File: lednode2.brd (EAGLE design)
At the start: 99.8 x 49.8 mm, 47 parts, among them Q1 AO3402, Q2 AO3402, Q3 AO3402, Q4 AO3402, Q5 AO3402, Q6 AO3402

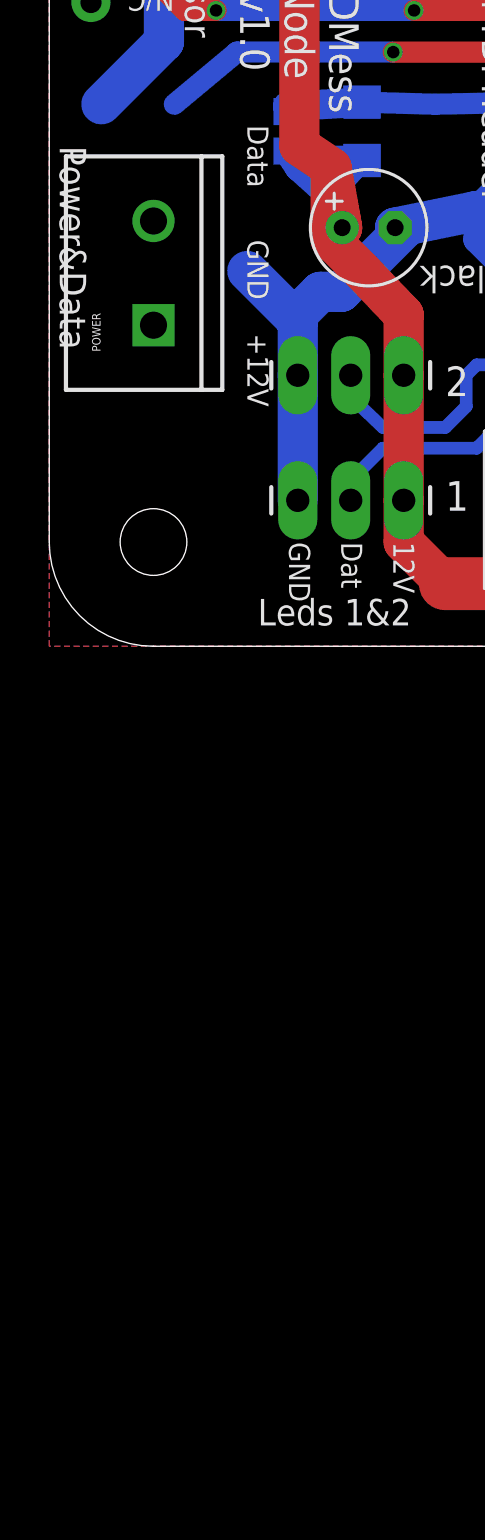
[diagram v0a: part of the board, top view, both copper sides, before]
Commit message: Working on new node version.
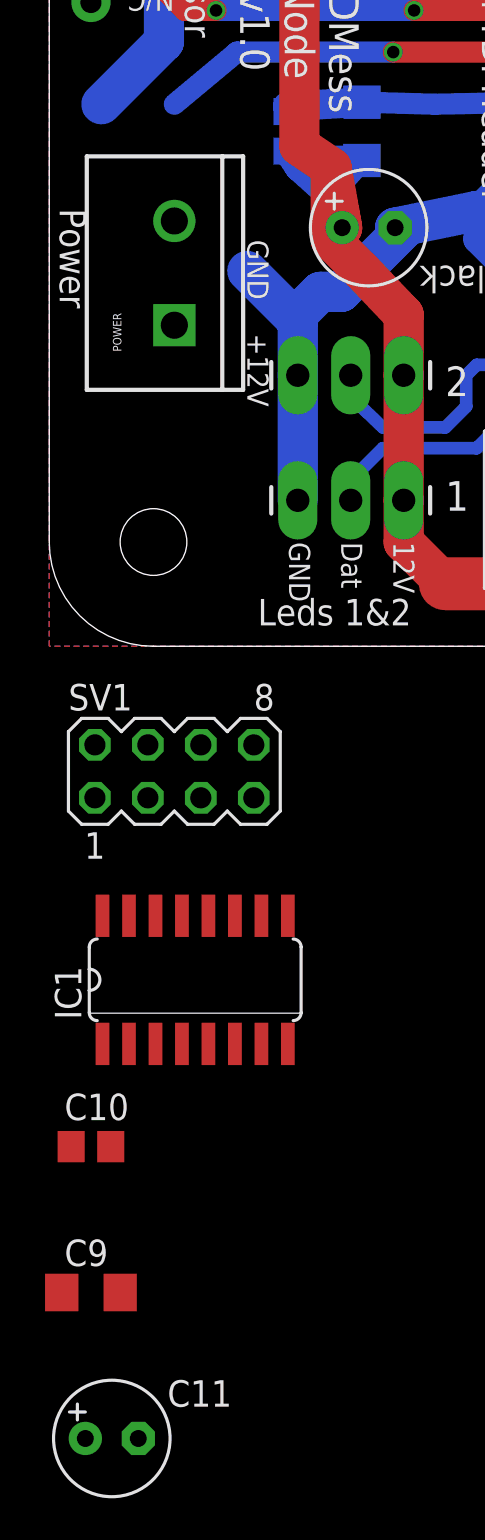
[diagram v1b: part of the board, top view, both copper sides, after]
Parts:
- added C10: 100 nF, rcl:C0805
- added C11: 100 uF, rcl:E2,5-6
- added C9: 10 uF, rcl:C1206
- added IC1: 74HCT595D, 74xx-eu:SO16
- added SV1: (no value), con-lstb:MA04-2
- moved POWER 1.00 mm to (6.00, 15.4)
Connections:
- new net +3V3: C10.1, C11.+, C9.1
- new net N$17: SV1.1
- new net N$18: SV1.3
- new net N$19: SV1.5
- new net N$20: SV1.7
- new net N$21: SV1.8
- new net N$22: SV1.6
- new net N$23: SV1.4
- new net N$24: SV1.2
- new net N$25: IC1.12
- new net N$26: IC1.11
- new net N$27: IC1.14
- new net VCC: IC1.16
- net GND: now also C10.2, C11.-, C9.2, IC1.8
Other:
- board text added: "Power"
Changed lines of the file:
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@@
 <text x="48.5" y="49" size="1.27" layer="112" font="vector" ratio="10" rot="SR180">Power&amp;Data</text>
 <text x="37.5" y="1" size="1.27" layer="112" font="vector" ratio="10" rot="SR0">Power&amp;Data</text>
-<text x="0.5" y="24" size="1.27" layer="112" font="vector" ratio="10" rot="SR270">Power&amp;Data</text>
+<text x="0.5" y="21" size="1.27" layer="112" font="vector" ratio="10" rot="SR270">Power</text>
 <text x="99" y="12" size="1.27" layer="112" font="vector" ratio="10" rot="SR90">Power&amp;Data</text>
 <text x="10" y="1" size="1.27" layer="112" font="vector" ratio="10">Leds 1&amp;2</text>
@@
 <text x="49.5" y="39" size="1.016" layer="112" font="vector" ratio="10" rot="SR180">Data</text>
 <text x="89.5" y="11.5" size="1.016" layer="112" font="vector" ratio="10" rot="SR90">Data</text>
-<text x="9.5" y="25" size="1.016" layer="112" font="vector" ratio="10" rot="SR270">Data</text>
 <text x="84" y="45.5" size="1.016" layer="112" font="vector" ratio="10" rot="R90">In</text>
 <text x="95.5" y="32.5" size="1.016" layer="112" font="vector" ratio="10">In</text>
@@
 <element name="RESET" library="SparkFun-Connectors" package="1X01NS" value="M01SMDNS" x="30.52" y="20.32"/>
 <element name="GND" library="SparkFun-Connectors" package="1X01NS" value="M01SMDNS" x="33.06" y="20.32"/>
-<element name="POWER" library="SparkFun" package="SCREWTERMINAL-5MM-2" value="" x="5" y="15.4" rot="R90"/>
+<element name="POWER" library="SparkFun" package="SCREWTERMINAL-5MM-2" value="" x="6" y="15.4" rot="R90"/>
+<element name="SV1" library="con-lstb" package="MA04-2" value="" x="6" y="-6">
+<attribute name="OC_NEWARK" value="unknown" x="6" y="-6" size="1.778" layer="27" display="off"/>
+<attribute name="MPN" value="" x="6" y="-6" size="1.778" layer="27" display="off"/>
+<attribute name="MF" value="" x="6" y="-6" size="1.778" layer="27" display="off"/>
+<attribute name="OC_FARNELL" value="unknown" x="6" y="-6" size="1.778" layer="27" display="off"/>
+</element>
+<element name="IC1" library="74xx-eu" package="SO16" value="74HCT595D" x="7" y="-16"/>
+<element name="C9" library="rcl" package="C1206" value="10 uF" x="2" y="-31"/>
+<element name="C10" library="rcl" package="C0805" value="100 nF" x="2" y="-24"/>
+<element name="C11" library="rcl" package="E2,5-6" value="100 uF" x="3" y="-38"/>
 </elements>
 <signals>
@@
 <wire x1="83.5" y1="10" x2="88" y2="10" width="1.016" layer="16"/>
 <contactref element="POWER" pad="1"/>
+<contactref element="IC1" pad="8"/>
+<contactref element="C9" pad="2"/>
+<contactref element="C10" pad="2"/>
+<contactref element="C11" pad="-"/>
+<wire x1="81.72" y1="12.3" x2="83.5" y2="10" width="0" layer="19" extent="16-16"/>
+<wire x1="17" y1="37" x2="17.08" y2="37" width="0" layer="19" extent="16-16"/>
+<wire x1="23" y1="26.05" x2="26.5" y2="28" width="0" layer="19" extent="16-16"/>
+<wire x1="27.5" y1="10" x2="25.6" y2="12.3" width="0" layer="19" extent="16-16"/>
+<wire x1="6" y1="15.4" x2="9.5" y2="18" width="0" layer="19" extent="16-16"/>
+<wire x1="11.445" y1="-19.0734" x2="11.92" y2="7" width="0" layer="19" extent="1-1"/>
+<wire x1="2.95" y1="-24" x2="11.445" y2="-19.0734" width="0" layer="19" extent="1-1"/>
+<wire x1="3.4" y1="-31" x2="2.95" y2="-24" width="0" layer="19" extent="1-1"/>
+<wire x1="4.27" y1="-38" x2="3.4" y2="-31" width="0" layer="19" extent="1-1"/>
 </signal>
 <signal name="+5V">
@@
 <wire x1="30.52" y1="20.32" x2="31.38" y2="17.38" width="1.016" layer="1"/>
 </signal>
+<signal name="N$17">
+<contactref element="SV1" pad="1"/>
+</signal>
+<signal name="N$18">
+<contactref element="SV1" pad="3"/>
+</signal>
+<signal name="N$19">
+<contactref element="SV1" pad="5"/>
+</signal>
+<signal name="N$20">
+<contactref element="SV1" pad="7"/>
+</signal>
+<signal name="N$21">
+<contactref element="SV1" pad="8"/>
+</signal>
+<signal name="N$22">
+<contactref element="SV1" pad="6"/>
+</signal>
+<signal name="N$23">
+<contactref element="SV1" pad="4"/>
+</signal>
+<signal name="N$24">
+<contactref element="SV1" pad="2"/>
+</signal>
+<signal name="VCC">
+<contactref element="IC1" pad="16"/>
+</signal>
+<signal name="N$25">
+<contactref element="IC1" pad="12"/>
+</signal>
+<signal name="N$26">
+<contactref element="IC1" pad="11"/>
+</signal>
+<signal name="N$27">
+<contactref element="IC1" pad="14"/>
+</signal>
+<signal name="+3V3">
+<contactref element="C9" pad="1"/>
+<contactref element="C10" pad="1"/>
+<contactref element="C11" pad="+"/>
+<wire x1="0.6" y1="-31" x2="1.73" y2="-38" width="0" layer="19" extent="1-1"/>
+<wire x1="1.05" y1="-24" x2="0.6" y2="-31" width="0" layer="19" extent="1-1"/>
+</signal>
 </signals>

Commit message: Working on lednode v2.0
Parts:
- removed IC1: 74HCT595D, 74xx-eu:SO16
- removed LEDS6: (no value), SparkFun-Connectors:1X03_LONGPADS
- removed Q6: AO3402, adafruit:SOT23-W
- removed R1, R2, R3: 10k, rcl:R0805
- removed SENSOR1, SENSOR2: (no value), SparkFun-Connectors:1X03
- removed SHAKE: SW-18010P, sensor-comus-group:CM4400
- removed SPOT6: M025MM, SparkFun-Connectors:SCREWTERMINAL-5MM-2
- removed SV1: (no value), con-lstb:MA04-2
- removed THERM: 10k, discrete-fixed-thermistor-silk:R-7,5
- added 3.3V_REGULATOR: AMS1117-3.3, burr-brown:SOT223
- added C12: 22uF, Tantalum, rcl:SMC_A
- added C13: (22uF, Tantalum), rcl:SMC_A
- added C14, C15: 100 uF, rcl:E2,5-6
- added IO1, IO2: (no value), SparkFun-Connectors:1X03
- added L1: WS2812B, adafruit:WS2812B
- added POWERLED: (no value), led:1206
- added RADIO: NRF24L01, con-lstb:MA04-2
- C9: value 10 uF -> 100 uF; device rcl:C1206 -> rcl:E2,5-6
- moved C11 86.6 mm to (31.0, 44.0), turned to 180 degrees
- moved C10 76.0 mm to (36.0, 44.0), flipped to the bottom, turned to 270 degrees
- moved LEDS3 52.0 mm to (35.0, 9.00)
- moved C9 48.8 mm to (15.0, 16.0), turned to 180 degrees
- moved LEDS4 43.2 mm to (44.0, 9.00)
- moved SPOT5 34.7 mm to (91.0, 36.0), turned to 270 degrees
- moved SPOT4 29.7 mm to (91.0, 22.0), turned to 270 degrees
- moved C2 28.8 mm to (43.7, 14.9), turned to 180 degrees
- moved SPOT1 28.1 mm to (57.0, 9.00)
- moved Q1 27.6 mm to (52.0, 13.0)
- moved Q4 24.6 mm to (86.0, 17.0), turned to 90 degrees
- moved PIR 24.3 mm to (73.5, 45.0), turned to 180 degrees
- moved Q5 24.2 mm to (85.0, 30.0), turned to 90 degrees
- moved SOUND_SENSOR 22.5 mm to (23.5, 45.0), turned to 180 degrees
- moved C1 16.2 mm to (70.5, 19.0), turned to 90 degrees
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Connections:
- net EXTRA_SENSOR1 renamed EXTRA_IO1
- net EXTRA_SENSOR2 renamed EXTRA_IO2
- removed net DATA_BUS: U$1.17
- removed net LEDSTRIP6: LEDS6.2, U$1.19
- removed net N$12: Q6.1, RN3.5
- removed net N$17: SV1.1
- removed net N$18: SV1.3
- removed net N$19: SV1.5
- removed net N$20: SV1.7
- removed net N$21: SV1.8
- removed net N$22: SV1.6
- removed net N$23: SV1.4
- removed net N$24: SV1.2
- removed net N$25: IC1.12
- removed net N$26: IC1.11
- removed net N$27: IC1.14
- removed net SHAKE: R1.2, SHAKE.1, U$1.15
- removed net SPOTLIGHT6: RN3.4, RN4.5, U$1.14
- removed net TEMPERATURE: R2.2, THERM.2, U$1.A6
- removed net VCC: IC1.16
- new net RADIO_CE: RADIO.3, U$1.18
- new net RADIO_CSN: RADIO.4, U$1.17
- new net RADIO_IRQ: RADIO.8
- new net RADIO_MISO: RADIO.7, U$1.15
- new net RADIO_MOSI: RADIO.6, U$1.14
- new net RADIO_SCK: RADIO.5, U$1.16
- new net STATUS_AND_LEDSTRIP5: L1.4-DIN, U$1.20
- net +12V: now also 3.3V_REGULATOR.3, C13.+, C14.+, C9.+; no longer LEDS6.1, SPOT6.1
- net +3V3: now also 3.3V_REGULATOR.2, C12.+, POWERLED.A, RADIO.2; no longer C9.1
- net +5V: now also C15.+, IO1.3, IO2.3, L1.1-VDD; no longer SENSOR1.3, SENSOR2.3, SHAKE.2, THERM.1
- net GND: now also 3.3V_REGULATOR.1, C12.-, C13.-, C14.-, C15.-, C9.-, IO1.1, IO2.1, L1.3-GND, RADIO.1, RN3.4; no longer C9.2, IC1.8, LEDS6.3, Q6.2, R1.1, R2.1, R3.1, SENSOR1.1, SENSOR2.1
- net LEDSTRIP1: now also U$1.5; no longer U$1.7
- net LEDSTRIP2: now also U$1.7; no longer U$1.5
- net LEDSTRIP5: now also L1.2-DOUT; no longer U$1.18
- net LIGHTLEVEL: now also RN4.5; no longer R3.2
- net N$11: now also POWERLED.C, RN3.5; no longer Q6.3, SPOT6.2
- net N$13: now also IO2.2; no longer SENSOR2.2
- net PROXIMITY: now also U$1.A6; no longer U$1.16
- net SENSOR1: now also IO1.2; no longer SENSOR1.2
- net SOUND_ANALOG: now also U$1.19; no longer U$1.20
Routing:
- net GND: track 472.1 -> 36.4 mm
- net +12V: track 318.3 -> 0.00 mm
- net DATA_BUS: track 137.1 -> 0.00 mm, vias 4 -> 0
- net +5V: track 136.6 -> 10.3 mm, vias 3 -> 0
- net SENSOR1: track 62.1 -> 0.00 mm
- net PROXIMITY: track 54.9 -> 0.00 mm
- net N$6: track 47.4 -> 0.00 mm, vias 2 -> 0
- net LEDSTRIP3: track 42.0 -> 0.00 mm
- net SOUND_ANALOG: track 41.4 -> 0.00 mm, vias 2 -> 0
- net N$12: track 40.5 -> 0.00 mm
- net LEDSTRIP4: track 38.6 -> 0.00 mm
- net SHAKE: track 38.4 -> 0.00 mm
- net LEDSTRIP5: track 33.9 -> 0.00 mm
- net N$13: track 59.0 -> 26.4 mm
- net LEDSTRIP1: track 32.4 -> 0.00 mm, vias 1 -> 0
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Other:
- board text added: "IN/OUT 1"
- board text added: "IN/OUT 2"
- board text added: "IO1"
- board text added: "IO2"
- board text added: "LEDMess Node v2.0"
- board text added: "LEDMess v2.0"
- board text added: "Leds 1"
- board text added: "Leds 2"
- board text added: "Leds 3"
- board text added: "Leds 4"
- board text added: "Leds 5"
- board text added: "Movement"
- board text added: "Programming Connector"
- board text added: "RED: Error YELLOW: No signal GREEN: Ok CYAN: Activity BLUE: Got Message PINK: Unconfigured"
- board text added: "Status"
- board text added: "TODO: Check size of * Sound sensor module * Radio module * PIR module And make sure they can be mounted at the same time (on top?)."
- board text removed: "3"
- board text removed: "4"
- board text removed: "6"
- board text removed: "Data"
- board text removed: "In"
- board text removed: "LDR Volt Div"
- board text removed: "LEDMess Node v1.0"
- board text removed: "Leds 1&2"
- board text removed: "Leds 3&4"
- board text removed: "Leds 5&6"
- board text removed: "Light Resistor"
- board text removed: "Power&Data"
- board text removed: "Sensors"
- board text removed: "Spot 6"
- board text removed: "Therm Volt Div"
- board text removed: "Thermistor"
- board text removed: "Vibration Pulldown"
- board text removed: "Vibration Switch"
- board text removed: "v1.0"

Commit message: tuning.
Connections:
- new net N$12: RN4.3, RN4.4
- new net N$17: RN4.6, RN4.7
- net GND: no longer RN4.3, RN4.4
- net N$13: no longer RN2.5
- net SENSOR1: no longer RN4.8
- net SPOTLIGHT4: now also RN2.5; no longer RN4.7
- net SPOTLIGHT5: now also RN4.8; no longer RN4.6
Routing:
- net GND: track 36.4 -> 29.4 mm
- net SPOTLIGHT4: track 35.5 -> 33.1 mm
- net N$13: track 26.4 -> 24.1 mm
- net SPOTLIGHT5: track 19.6 -> 18.4 mm
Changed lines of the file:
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@@
 <contactref element="LEDS5" pad="3"/>
 <contactref element="Q5" pad="2"/>
-<contactref element="RN4" pad="3"/>
-<contactref element="RN4" pad="2"/>
-<contactref element="RN4" pad="1"/>
-<contactref element="RN2" pad="4"/>
-<wire x1="39.025" y1="28.9" x2="39.025" y2="28.1" width="0.6096" layer="16"/>
-<wire x1="39.025" y1="28.1" x2="39.025" y2="27.205" width="0.6096" layer="16"/>
 <wire x1="39.025" y1="22.705" x2="39.025" y2="23.6" width="0.6096" layer="16"/>
 <wire x1="39.025" y1="23.6" x2="39.025" y2="24.4" width="0.6096" layer="16"/>
-<wire x1="39.025" y1="24.4" x2="39.025" y2="25.295" width="0.6096" layer="16"/>
-<wire x1="39.025" y1="25.295" x2="39.025" y2="27.205" width="0.6096" layer="16"/>
-<wire x1="39.025" y1="27.205" x2="37" y2="25.705" width="0.6096" layer="16"/>
 <wire x1="37" y1="25.705" x2="32.395" y2="25.705" width="1.27" layer="16"/>
 <wire x1="32.395" y1="25.705" x2="31.6" y2="29" width="0.6096" layer="16"/>
@@
 <contactref element="C13" pad="-"/>
 <contactref element="C12" pad="-"/>
-<contactref element="RN4" pad="4"/>
 <contactref element="RN3" pad="4"/>
 <contactref element="C14" pad="-"/>
@@
 <contactref element="C15" pad="-"/>
 <contactref element="L1" pad="3-GND"/>
-<wire x1="70.5" y1="20.27" x2="60.025" y2="30.295" width="0" layer="19" extent="16-16"/>
-<wire x1="39.025" y1="29.795" x2="39.025" y2="28.9" width="0" layer="19" extent="16-16"/>
-<wire x1="12.35" y1="33.55" x2="7.5" y2="36.08" width="0" layer="19" extent="1-1"/>
+<contactref element="RN4" pad="1"/>
+<contactref element="RN2" pad="4"/>
+<contactref element="RN4" pad="2"/>
+<wire x1="73.5" y1="45" x2="86" y2="45" width="0" layer="19" extent="1-1"/>
+<wire x1="76.27" y1="37" x2="73.5" y2="45" width="0" layer="19" extent="1-1"/>
+<wire x1="83.7" y1="31.1" x2="76.27" y2="37" width="0" layer="19" extent="16-16"/>
+<wire x1="80.73" y1="23" x2="83.7" y2="31.1" width="0" layer="19" extent="16-16"/>
+<wire x1="79.55" y1="20" x2="80.73" y2="23" width="0" layer="19" extent="16-16"/>
+<wire x1="84.7" y1="18.1" x2="79.55" y2="20" width="0" layer="19" extent="16-16"/>
+<wire x1="81.1" y1="14.3" x2="84.7" y2="18.1" width="0" layer="19" extent="16-16"/>
+<wire x1="74" y1="19.4" x2="79.55" y2="20" width="0" layer="19" extent="16-16"/>
+<wire x1="70.5" y1="20.27" x2="74" y2="19.4" width="0" layer="19" extent="16-16"/>
+<wire x1="67.1" y1="14.3" x2="70.5" y2="20.27" width="0" layer="19" extent="16-16"/>
+<wire x1="61" y1="45" x2="73.5" y2="45" width="0" layer="19" extent="1-1"/>
+<wire x1="53.1" y1="14.3" x2="67.1" y2="14.3" width="0" layer="19" extent="16-16"/>
+<wire x1="42.41" y1="14.92" x2="53.1" y2="14.3" width="0" layer="19" extent="16-16"/>
+<wire x1="38.92" y1="9" x2="42.41" y2="14.92" width="0" layer="19" extent="1-1"/>
+<wire x1="36.92" y1="20.38" x2="42.41" y2="14.92" width="0" layer="19" extent="16-16"/>
+<wire x1="39.025" y1="22.705" x2="37.42" y2="23.08" width="0" layer="19" extent="16-16"/>
+<wire x1="39.025" y1="25.295" x2="39.025" y2="24.4" width="0" layer="19" extent="16-16"/>
+<wire x1="39.025" y1="27.205" x2="39.025" y2="25.295" width="0" layer="19" extent="16-16"/>
+<wire x1="39.025" y1="28.1" x2="39.025" y2="27.205" width="0" layer="19" extent="16-16"/>
+<wire x1="36" y1="43.05" x2="31.84" y2="35.62" width="0" layer="19" extent="16-16"/>
+<wire x1="40.19" y1="42.73" x2="36" y2="43.05" width="0" layer="19" extent="16-16"/>
+<wire x1="29.73" y1="44" x2="36" y2="43.05" width="0" layer="19" extent="16-16"/>
+<wire x1="20.96" y1="45" x2="29.73" y2="44" width="0" layer="19" extent="1-1"/>
+<wire x1="29.92" y1="9" x2="38.92" y2="9" width="0" layer="19" extent="1-1"/>
+<wire x1="20.92" y1="9" x2="29.92" y2="9" width="0" layer="19" extent="1-1"/>
+<wire x1="11.92" y1="9" x2="20.92" y2="9" width="0" layer="19" extent="1-1"/>
+<wire x1="13.73" y1="16" x2="11.92" y2="9" width="0" layer="19" extent="1-1"/>
+<wire x1="12.9" y1="21" x2="13.73" y2="16" width="0" layer="19" extent="16-16"/>
+<wire x1="13.35" y1="24.5" x2="12.9" y2="21" width="0" layer="19" extent="16-16"/>
+<wire x1="15" y1="27.5" x2="13.35" y2="24.5" width="0" layer="19" extent="16-16"/>
+<wire x1="18" y1="27.5" x2="15" y2="27.5" width="0" layer="19" extent="16-16"/>
+<wire x1="7.5" y1="16.4" x2="13.73" y2="16" width="0" layer="19" extent="1-1"/>
+<wire x1="12.35" y1="33.55" x2="15" y2="27.5" width="0" layer="19" extent="1-16"/>
+<wire x1="7.5" y1="36.08" x2="12.35" y2="33.55" width="0" layer="19" extent="1-1"/>
+<wire x1="20.2606" y1="33.8504" x2="18" y2="27.5" width="0" layer="19" extent="16-16"/>
+<wire x1="60.025" y1="30.295" x2="70.5" y2="20.27" width="0" layer="19" extent="16-16"/>
 </signal>
 <signal name="+5V">
@@
 <signal name="SPOTLIGHT4">
 <contactref element="RN3" pad="2"/>
-<contactref element="RN4" pad="7"/>
 <wire x1="57.24" y1="20.76" x2="55.5" y2="22.5" width="0.6096" layer="1"/>
 <wire x1="55.5" y1="22.5" x2="52.5" y2="22.5" width="0.6096" layer="1"/>
 <wire x1="52.5" y1="22.5" x2="49" y2="26" width="0.6096" layer="1"/>
 <wire x1="49" y1="26" x2="46" y2="26" width="0.6096" layer="1"/>
-<wire x1="40.975" y1="28.1" x2="43.4" y2="28.1" width="0.4064" layer="16"/>
 <wire x1="43.4" y1="28.1" x2="44" y2="28" width="0.4064" layer="16"/>
 <via x="44" y="28" extent="1-16" drill="0.6" shape="octagon"/>
@@
 <wire x1="58" y1="28" x2="44" y2="28" width="0.4064" layer="16"/>
 <contactref element="U$1" pad="12"/>
+<contactref element="RN2" pad="5"/>
 <wire x1="57.24" y1="20.76" x2="57.24" y2="20.38" width="0" layer="19" extent="1-1"/>
+<wire x1="40.975" y1="25.295" x2="43.4" y2="28.1" width="0" layer="19" extent="16-16"/>
 </signal>
 <signal name="LIGHTLEVEL">
@@
 <signal name="SPOTLIGHT5">
 <contactref element="RN3" pad="3"/>
-<contactref element="RN4" pad="6"/>
 <wire x1="57.24" y1="29.24" x2="57" y2="29" width="0.6096" layer="1"/>
 <via x="57" y="29" extent="1-16" drill="0.6" shape="octagon"/>
@@
 <wire x1="60.025" y1="29.4" x2="57.4" y2="29.4" width="0.4064" layer="16"/>
 <wire x1="57.4" y1="29.4" x2="57" y2="29" width="0.4064" layer="16"/>
-<wire x1="40.975" y1="28.9" x2="42.15" y2="28.9" width="0.4064" layer="16"/>
 <wire x1="42.15" y1="28.9" x2="43.25" y2="29" width="0.4064" layer="16"/>
 <contactref element="U$1" pad="13"/>
+<contactref element="RN4" pad="8"/>
 <wire x1="57.4" y1="29.4" x2="57.24" y2="35.62" width="0" layer="19" extent="16-16"/>
+<wire x1="40.975" y1="27.205" x2="42.15" y2="28.9" width="0" layer="19" extent="16-16"/>
 </signal>
 <signal name="SENSOR1">
 <contactref element="IO1" pad="2"/>
-<contactref element="RN4" pad="8"/>
 <contactref element="RN3" pad="1"/>
 <wire x1="60.025" y1="27.705" x2="58.46" y2="45" width="0" layer="19" extent="16-16"/>
-<wire x1="40.975" y1="27.205" x2="60.025" y2="27.705" width="0" layer="19" extent="16-16"/>
 </signal>
 <signal name="N$8">
@@
 <signal name="N$13">
 <contactref element="IO2" pad="2"/>
-<contactref element="RN2" pad="5"/>
 <contactref element="RN1" pad="4"/>
 <wire x1="61.525" y1="24.295" x2="60.705" y2="24.295" width="0.4064" layer="16"/>
 <wire x1="60.705" y1="24.295" x2="60" y2="25" width="0.4064" layer="16"/>
 <wire x1="60" y1="25" x2="51.5" y2="25" width="0.4064" layer="16"/>
-<wire x1="40.975" y1="25.295" x2="43.25" y2="25.75" width="0.4064" layer="16"/>
 <wire x1="43.25" y1="25.75" x2="50.75" y2="25.75" width="0.4064" layer="16"/>
 <wire x1="50.75" y1="25.75" x2="51.5" y2="25" width="0.4064" layer="16"/>
@@
 <wire x1="15.65" y1="33.55" x2="39.46" y2="35.62" width="0" layer="19" extent="1-1"/>
 </signal>
+<signal name="N$12">
+<contactref element="RN4" pad="4"/>
+<contactref element="RN4" pad="3"/>
+<wire x1="39.025" y1="28.9" x2="39.025" y2="29.795" width="0" layer="19" extent="16-16"/>
+</signal>
+<signal name="N$17">
+<contactref element="RN4" pad="6"/>
+<contactref element="RN4" pad="7"/>
+<wire x1="40.975" y1="28.1" x2="40.975" y2="28.9" width="0" layer="19" extent="16-16"/>
+</signal>
 </signals>
